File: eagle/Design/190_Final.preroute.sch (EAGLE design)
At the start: 28 parts, among them U1_0_BRAIN ADAFRUIT-PRO-TRINKET-5V-BOB, U1_6_CASTER CASTERADAFRUIT-3/4IN, U1_7_CASTER_2 CASTERADAFRUIT-3/4IN

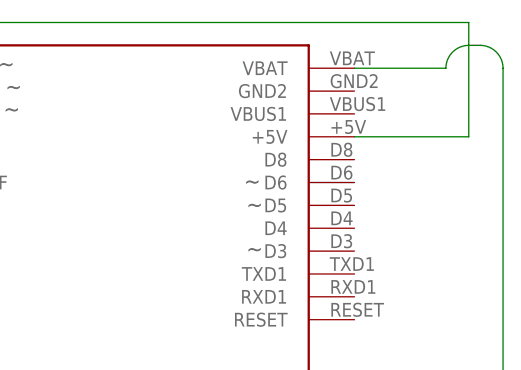
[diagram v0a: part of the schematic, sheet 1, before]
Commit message: caught a nasty electric bug
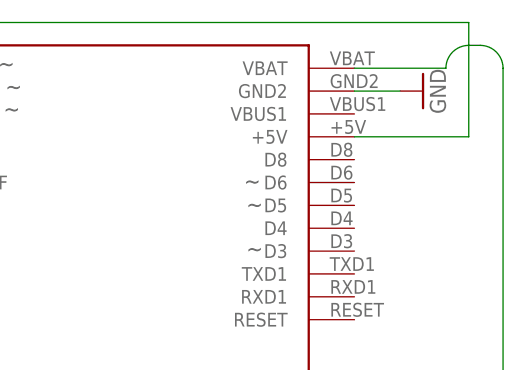
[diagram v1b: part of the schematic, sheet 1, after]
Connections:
- net GND: no longer U$2.C, U$2.K, U$3.C, U$3.K
- net GND_0_BRAIN: now also U$2.C, U$2.K, U$3.C, U$3.K
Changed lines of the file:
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@@
 <setting verticaltext="up"/>
 </settings>
-<grid distance="0.05" unitdist="inch" unit="inch" style="lines" multiple="1" display="no" altdistance="0.01" altunitdist="inch" altunit="inch"/>
+<grid distance="0.1" unitdist="inch" unit="inch" style="lines" multiple="1" display="no" altdistance="0.01" altunitdist="inch" altunit="inch"/>
 <layers>
 <layer number="1" name="Top" color="4" fill="1" visible="no" active="no"/>
@@
 <part name="U$2" library="SparkFun-Sensors" deviceset="QRD1114" device=""/>
 <part name="U$3" library="SparkFun-Sensors" deviceset="QRD1114" device=""/>
-<part name="GND1" library="supply1" deviceset="GND" device=""/>
+<part name="GND_0_BRAIN" library="supply1" deviceset="GND" device=""/>
 <part name="GND2" library="supply1" deviceset="GND" device=""/>
 <part name="GND3" library="supply1" deviceset="GND" device=""/>
@@
 <part name="R6" library="resistor" deviceset="R-US_" device="0204/7"/>
 <part name="GND5" library="supply1" deviceset="GND" device=""/>
+<part name="GND6" library="supply1" deviceset="GND" device=""/>
 </parts>
 <sheets>
@@
 <instance part="U$2" gate="G$1" x="-68.58" y="2.54"/>
 <instance part="U$3" gate="G$1" x="-68.58" y="-43.18"/>
-<instance part="GND1" gate="1" x="-66.04" y="-58.42"/>
+<instance part="GND_0_BRAIN" gate="1" x="-66.04" y="-58.42"/>
 <instance part="GND2" gate="1" x="-73.66" y="-58.42"/>
 <instance part="GND3" gate="1" x="-73.66" y="-12.7"/>
@@
 <instance part="R6" gate="G$1" x="-30.48" y="-40.64" rot="R270"/>
 <instance part="GND5" gate="1" x="-30.48" y="-12.7" rot="R180"/>
+<instance part="GND6" gate="1" x="33.02" y="17.78" rot="R90"/>
 </instances>
 <busses>
@@
 </segment>
 <segment>
+<pinref part="U$3" gate="G$1" pin="K"/>
+<wire x1="-73.66" y1="-50.8" x2="-73.66" y2="-55.88" width="0.1524" layer="91"/>
+<pinref part="GND2" gate="1" pin="GND"/>
+</segment>
+<segment>
+<pinref part="U$2" gate="G$1" pin="C"/>
+<wire x1="-66.04" y1="-5.08" x2="-66.04" y2="-10.16" width="0.1524" layer="91"/>
+<pinref part="GND4" gate="1" pin="GND"/>
+</segment>
+<segment>
+<pinref part="U$2" gate="G$1" pin="K"/>
+<wire x1="-73.66" y1="-5.08" x2="-73.66" y2="-10.16" width="0.1524" layer="91"/>
+<pinref part="GND3" gate="1" pin="GND"/>
+</segment>
+<segment>
+<pinref part="U$3" gate="G$1" pin="C"/>
+<wire x1="-66.04" y1="-50.8" x2="-66.04" y2="-55.88" width="0.1524" layer="91"/>
+<pinref part="GND_0_BRAIN" gate="1" pin="GND"/>
+</segment>
+<segment>
 <pinref part="U1_0_BRAIN" gate="G$1" pin="GND2"/>
+<wire x1="25.4" y1="17.78" x2="30.48" y2="17.78" width="0.1524" layer="91"/>
+<pinref part="GND6" gate="1" pin="GND"/>
 </segment>
 </net>
@@
 <net name="GND" class="0">
 <segment>
-<pinref part="U$3" gate="G$1" pin="C"/>
-<wire x1="-66.04" y1="-50.8" x2="-66.04" y2="-55.88" width="0.1524" layer="91"/>
-<pinref part="GND1" gate="1" pin="GND"/>
-</segment>
-<segment>
-<pinref part="U$3" gate="G$1" pin="K"/>
-<wire x1="-73.66" y1="-50.8" x2="-73.66" y2="-55.88" width="0.1524" layer="91"/>
-<pinref part="GND2" gate="1" pin="GND"/>
-</segment>
-<segment>
-<pinref part="U$2" gate="G$1" pin="K"/>
-<wire x1="-73.66" y1="-5.08" x2="-73.66" y2="-10.16" width="0.1524" layer="91"/>
-<pinref part="GND3" gate="1" pin="GND"/>
-</segment>
-<segment>
-<pinref part="U$2" gate="G$1" pin="C"/>
-<wire x1="-66.04" y1="-5.08" x2="-66.04" y2="-10.16" width="0.1524" layer="91"/>
-<pinref part="GND4" gate="1" pin="GND"/>
-</segment>
-<segment>
 <pinref part="R5" gate="G$1" pin="1"/>

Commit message: more electrical bug catches
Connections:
- removed net GND: R5.1
- net GND_0_BRAIN: now also R5.1
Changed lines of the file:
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@@
 <pinref part="GND6" gate="1" pin="GND"/>
+</segment>
+<segment>
+<pinref part="R5" gate="G$1" pin="1"/>
+<wire x1="-30.48" y1="-17.78" x2="-30.48" y2="-15.24" width="0.1524" layer="91"/>
+<pinref part="GND5" gate="1" pin="GND"/>
 </segment>
 </net>
@@
 </segment>
 </net>
-<net name="GND" class="0">
-<segment>
-<pinref part="R5" gate="G$1" pin="1"/>
-<wire x1="-30.48" y1="-17.78" x2="-30.48" y2="-15.24" width="0.1524" layer="91"/>
-<pinref part="GND5" gate="1" pin="GND"/>
-</segment>
-</net>
